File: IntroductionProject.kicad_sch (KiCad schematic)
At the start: 1 part

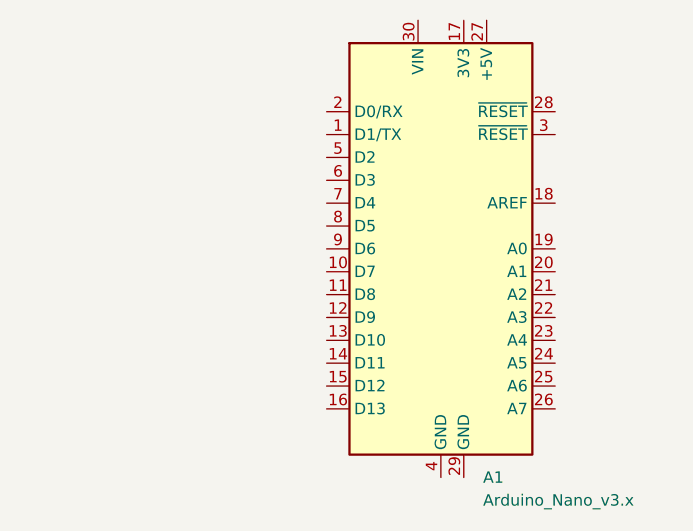
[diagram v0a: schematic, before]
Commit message: Updated BMP and MicroSD footprints to reflect courtyards and microSD card size
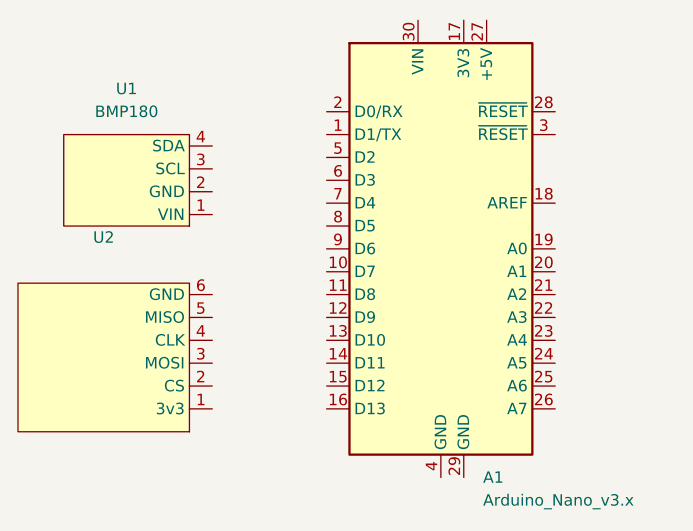
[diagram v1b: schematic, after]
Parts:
- added U1: BMP180, Components:BMP180, symbol Components:BMP180
- added U2: ~, Components:MicroSD, symbol Components:MicroSD
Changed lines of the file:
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@@
+		)
+	)
+	(symbol
+		(lib_id "Components:MicroSD")
+		(at 107.95 107.95 180)
+		(unit 1)
+		(exclude_from_sim no)
+		(in_bom yes)
+		(on_board yes)
+		(dnp no)
+		(fields_autoplaced yes)
+		(property "Reference" "U2"
+			(at 108.585 86.36 0)
+			(effects
+				(font
+					(size 1.27 1.27)
+				)
+			)
+		)
+		(property "Value" "~"
+			(at 108.585 88.9 0)
+			(effects
+				(font
+					(size 1.27 1.27)
+				)
+			)
+		)
+		(property "Footprint" "Components:MicroSD"
+			(at 107.95 107.95 0)
+			(effects
+				(font
+					(size 1.27 1.27)
+				)
+				(hide yes)
+			)
+		)
+		(property "Datasheet" ""
+			(at 107.95 107.95 0)
+			(effects
+				(font
+					(size 1.27 1.27)
+				)
+				(hide yes)
+			)
+		)
+		(property "Description" ""
+			(at 107.95 107.95 0)
+			(effects
+				(font
+					(size 1.27 1.27)
+				)
+				(hide yes)
+			)
+		)
+		(pin "4"
+		)
+		(pin "3"
+		)
+		(pin "6"
+		)
+		(pin "5"
+		)
+		(pin "2"
+		)
+		(pin "1"
+		)
+		(instances
+			(project ""
+				(path "/8c127b91-fe28-4423-8567-ad0a7d5ca14e"
+					(reference "U2")
+					(unit 1)
+				)
+			)
+		)
+	)
+	(symbol
+		(lib_id "Components:BMP180")
+		(at 110.49 81.28 180)
+		(unit 1)
+		(exclude_from_sim no)
+		(in_bom yes)
+		(on_board yes)
+		(dnp no)
+		(fields_autoplaced yes)
+		(property "Reference" "U1"
+			(at 111.125 69.85 0)
+			(effects
+				(font
+					(size 1.27 1.27)
+				)
+			)
+		)
+		(property "Value" "BMP180"
+			(at 111.125 72.39 0)
+			(effects
+				(font
+					(size 1.27 1.27)
+				)
+			)
+		)
+		(property "Footprint" "Components:BMP180"
+			(at 110.49 72.39 0)
+			(effects
+				(font
+					(size 1.27 1.27)
+				)
+				(hide yes)
+			)
+		)
+		(property "Datasheet" ""
+			(at 110.49 72.39 0)
+			(effects
+				(font
+					(size 1.27 1.27)
+				)
+				(hide yes)
+			)
+		)
+		(property "Description" ""
+			(at 110.49 72.39 0)
+			(effects
+				(font
+					(size 1.27 1.27)
+				)
+				(hide yes)
+			)
+		)
+		(pin "1"
+		)
+		(pin "2"
+		)
+		(pin "3"
+		)
+		(pin "4"
+		)
+		(instances
+			(project ""
+				(path "/8c127b91-fe28-4423-8567-ad0a7d5ca14e"
+					(reference "U1")
+					(unit 1)
+				)
+			)
 		)
 	)
